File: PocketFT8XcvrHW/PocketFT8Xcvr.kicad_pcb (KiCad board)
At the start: 4 copper layers, 101.6 x 69.9 mm, 58 parts, among them IC1 SI5351C-B-GM1, J1 HX8357D SPI, J2 22-23-2021, J3 GPS, J5 HX8357D 8-BIT, Q1 2N3904, Q2 2N3906, Q3 2N7000, Q4 2N7000, U1 MCP3422A1T-E/SN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

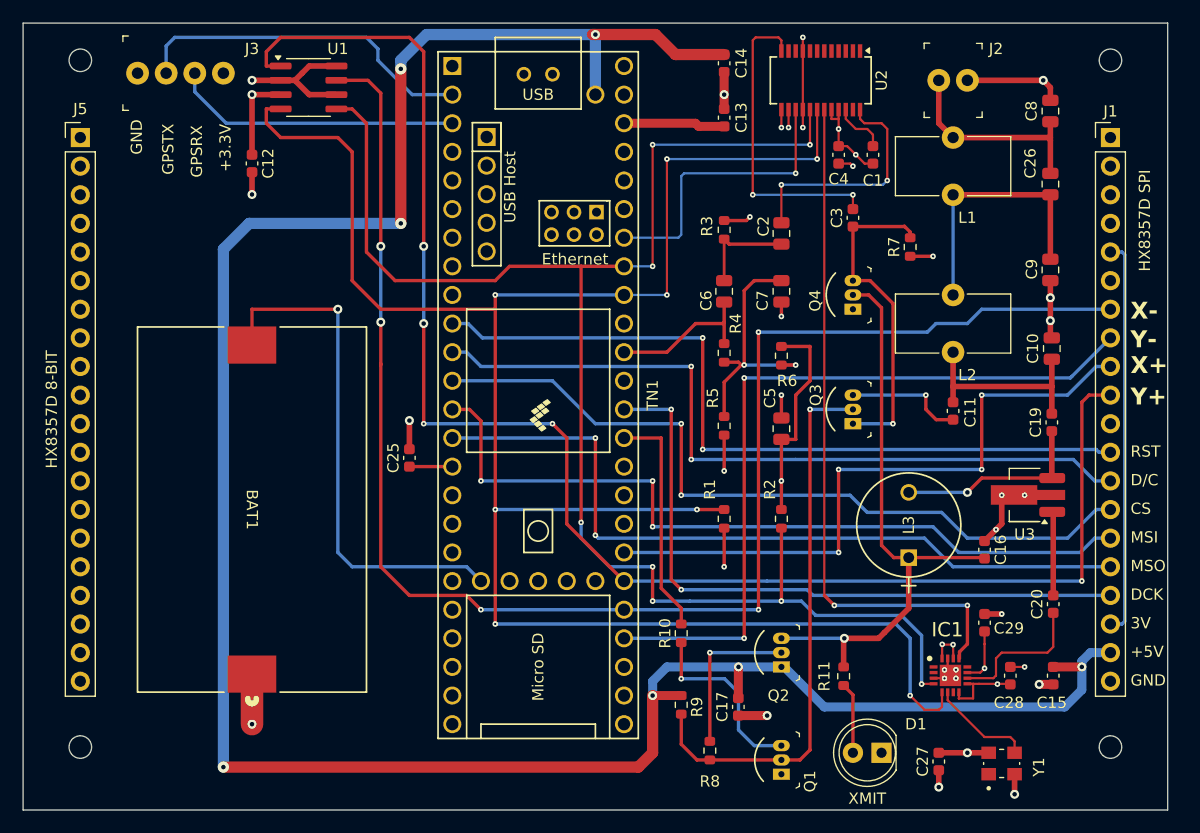
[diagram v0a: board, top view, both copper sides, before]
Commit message: Housecleaning after abandoning the QFN16 SI5351 package
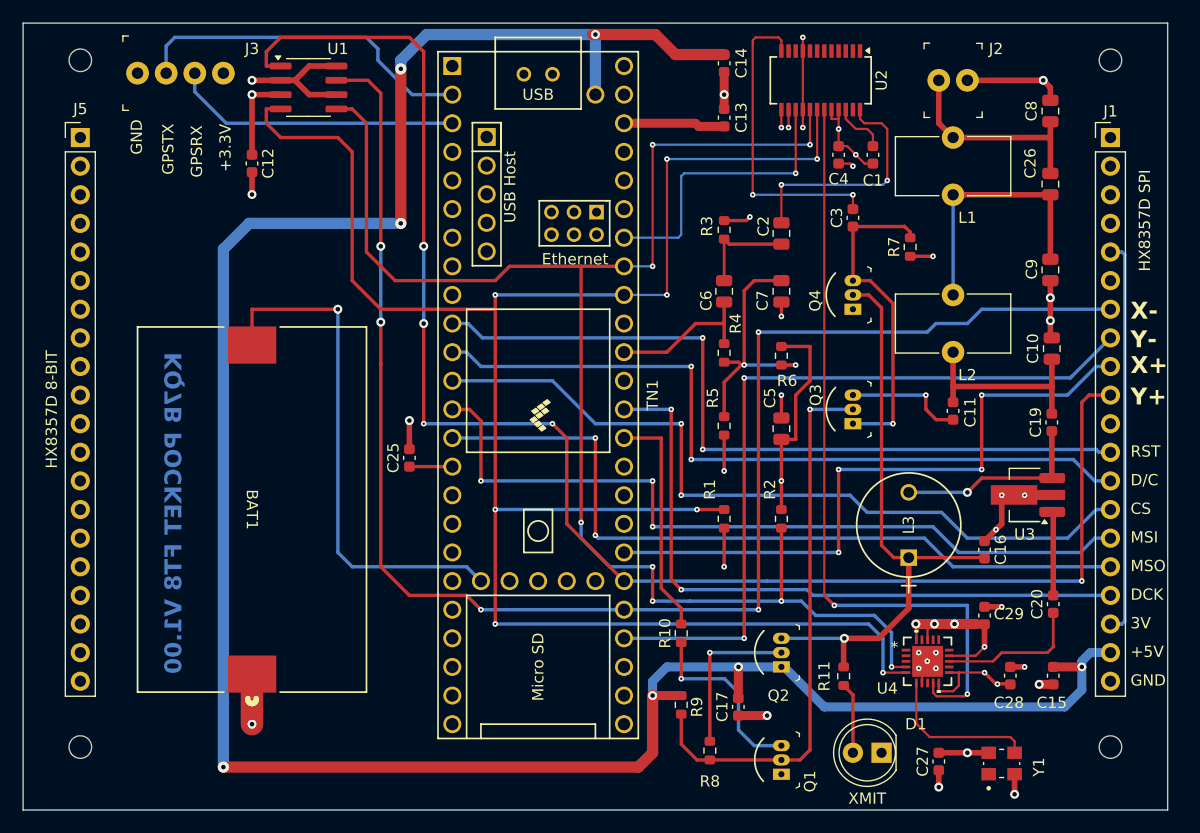
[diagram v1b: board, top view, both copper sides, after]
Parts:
- removed IC1: SI5351C-B-GM1, SI5351C-B-GM1:QFN50P300X300X90-17N-D
- added U4: SI5351C-B-GM, SI5351C-B-GM:QFN20_4X4_SKY, F.Cu at (181.9, 107.5)
- moved C29 0.63 mm to (186.9, 103.4)
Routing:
- net +3.3V: track 71.3 -> 79.9 mm, vias 10 -> 12
- net /SDA: track 178.1 -> 171.0 mm
- net /RCLK: track 61.2 -> 68.2 mm
- net Net-(U4-CLKIN): track 9.17 -> 14.0 mm
- net /SCL: track 141.1 -> 137.2 mm
- net GND: track 80.7 -> 80.0 mm, vias 31 -> 32
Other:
- board text added: "KQ7B POCKET FT8 V1.00"

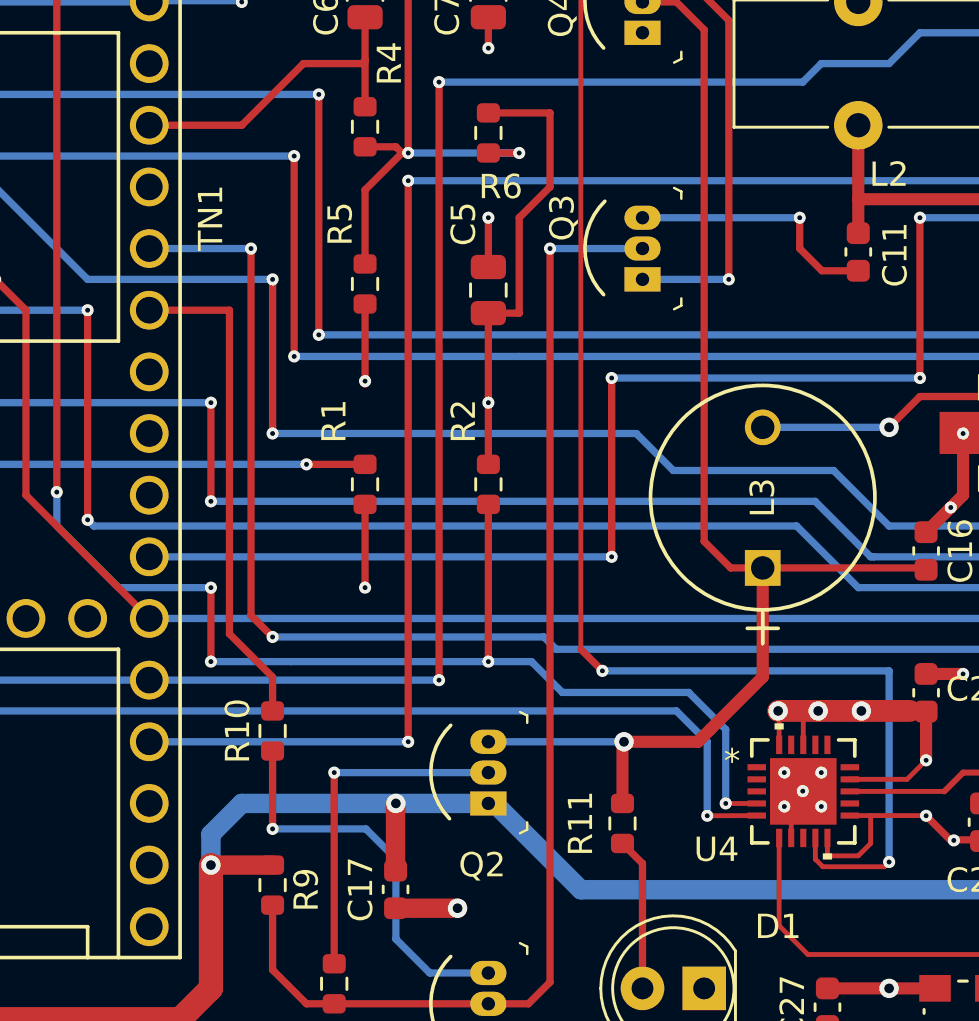
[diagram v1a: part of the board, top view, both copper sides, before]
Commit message: PCB Patch, test and FW changes to repair 1-v101-sck-and-ptt-reversed
SCK signal moved from digital pin 14 in Teensy 3.6 to pin 13 in Teensy 4.1.  Workaround PCB patch swaps pins 13 and 14.  Schematic, board layout, tests and FW updated for revised pin assignments.  Test03-Display now passes.
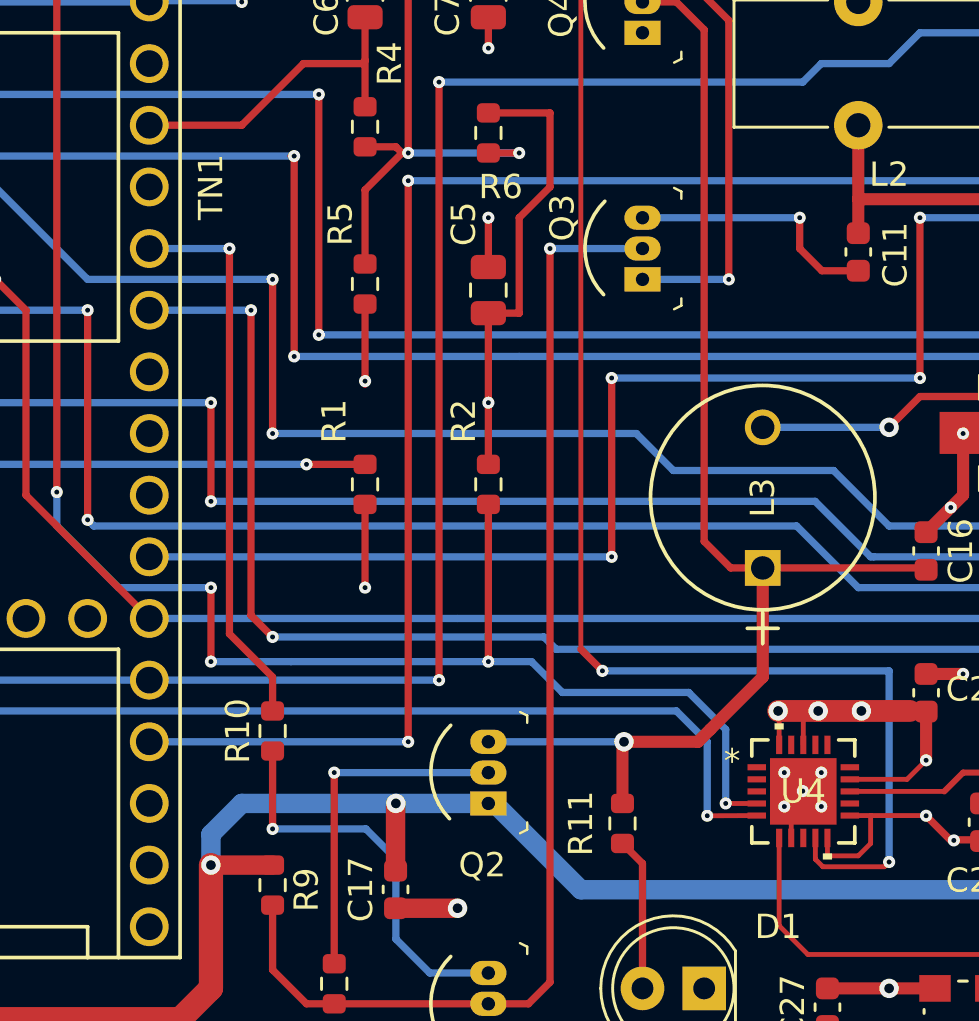
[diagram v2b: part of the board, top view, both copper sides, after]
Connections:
- TN1 pad 35: /PTT -> /DCLK
- TN1 pad 36: /DCLK -> /PTT
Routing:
- net /PTT: track 20.5 -> 23.1 mm, vias 0 -> 1
- net /DCLK: track 58.9 -> 56.3 mm

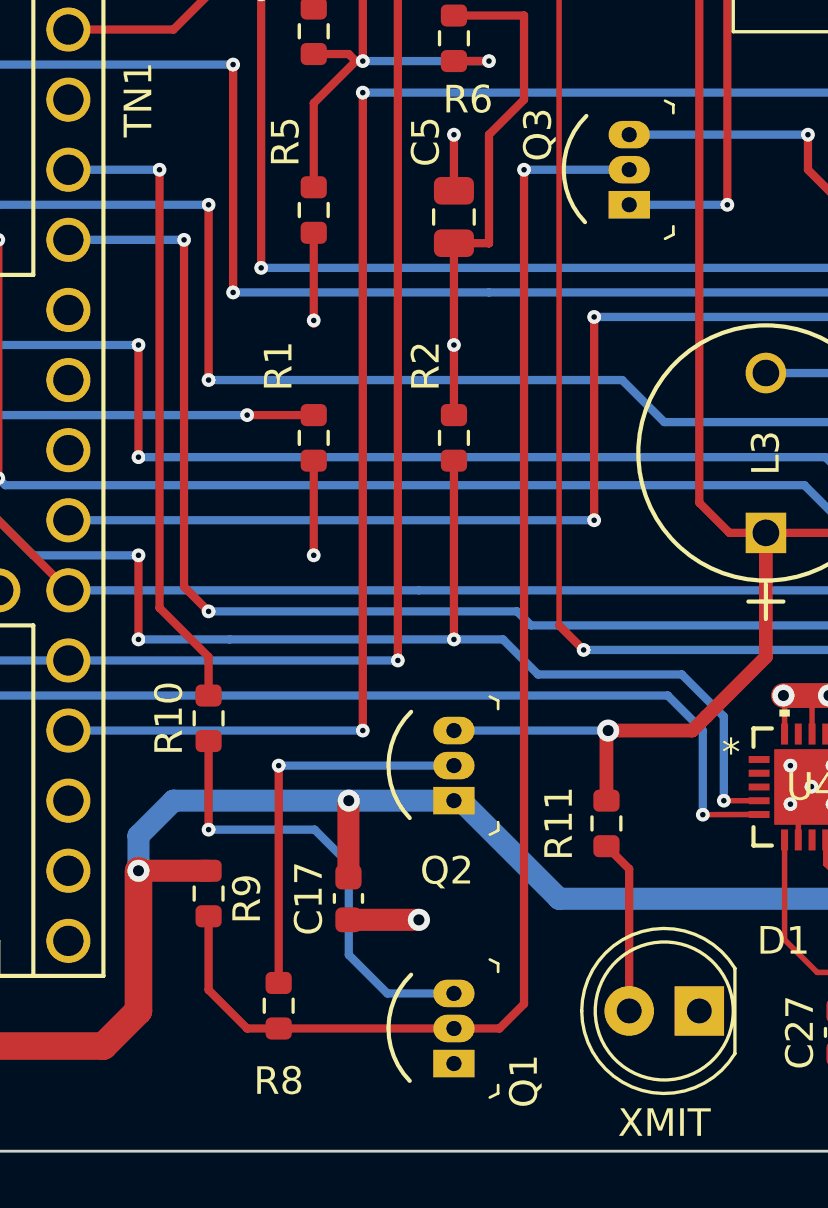
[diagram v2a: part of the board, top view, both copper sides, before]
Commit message: Fixed XMIT LED is always "on" and cannot be turned-off
The digikey 2N3904 symbol reversed the pin numbers for B and C.  This commit includes the schematic with the corrected symbol.
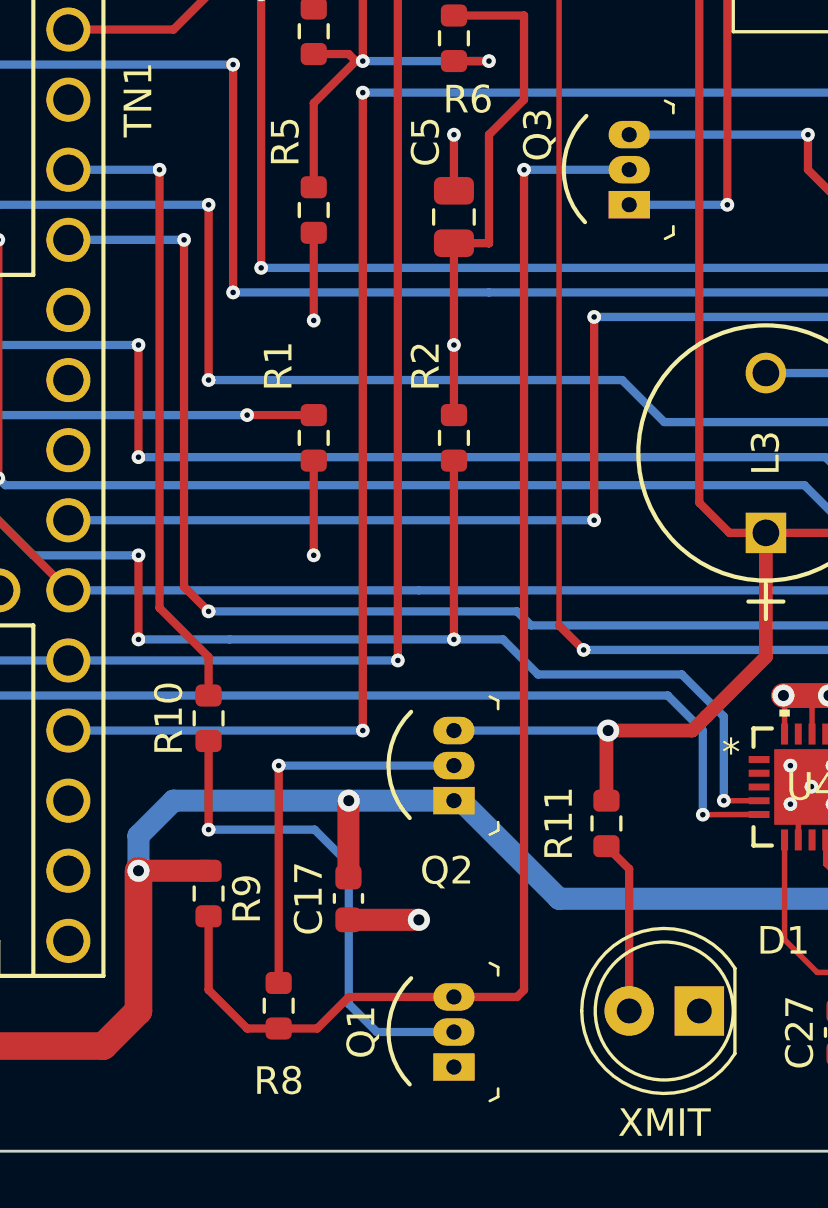
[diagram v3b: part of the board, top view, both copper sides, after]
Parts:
- moved Q1 0.13 mm to (168.9, 117.6)
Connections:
- Q1 pad 2: /RECV -> Net-(Q1-B)
- Q1 pad 3: Net-(Q1-B) -> /RECV
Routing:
- net Net-(Q1-B): track 16.5 -> 18.1 mm

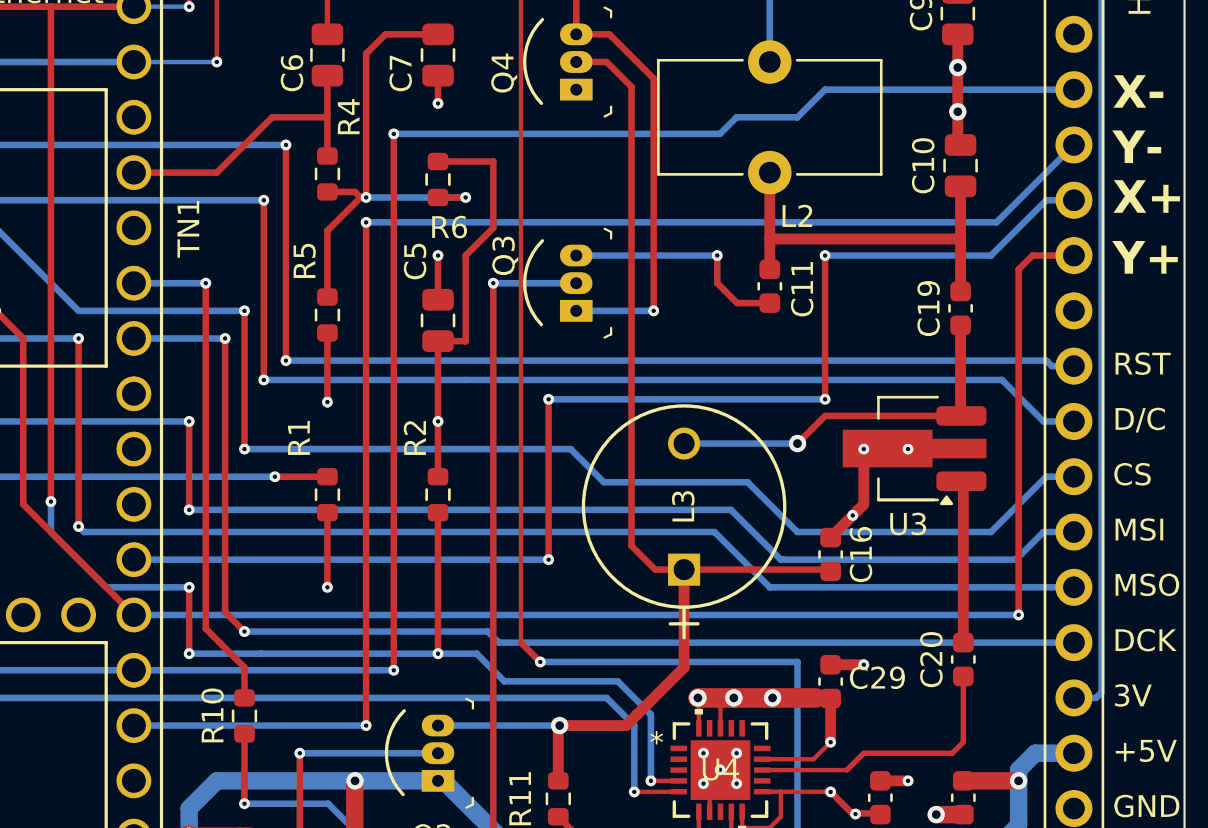
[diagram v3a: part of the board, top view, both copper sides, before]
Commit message: Resolved:  Touchpad needs coordination over full screen #8
Added R12 and R13 to lower the driven voltage to the touchpad so that it lies below the MCP3422's 2.048 Volt reference.
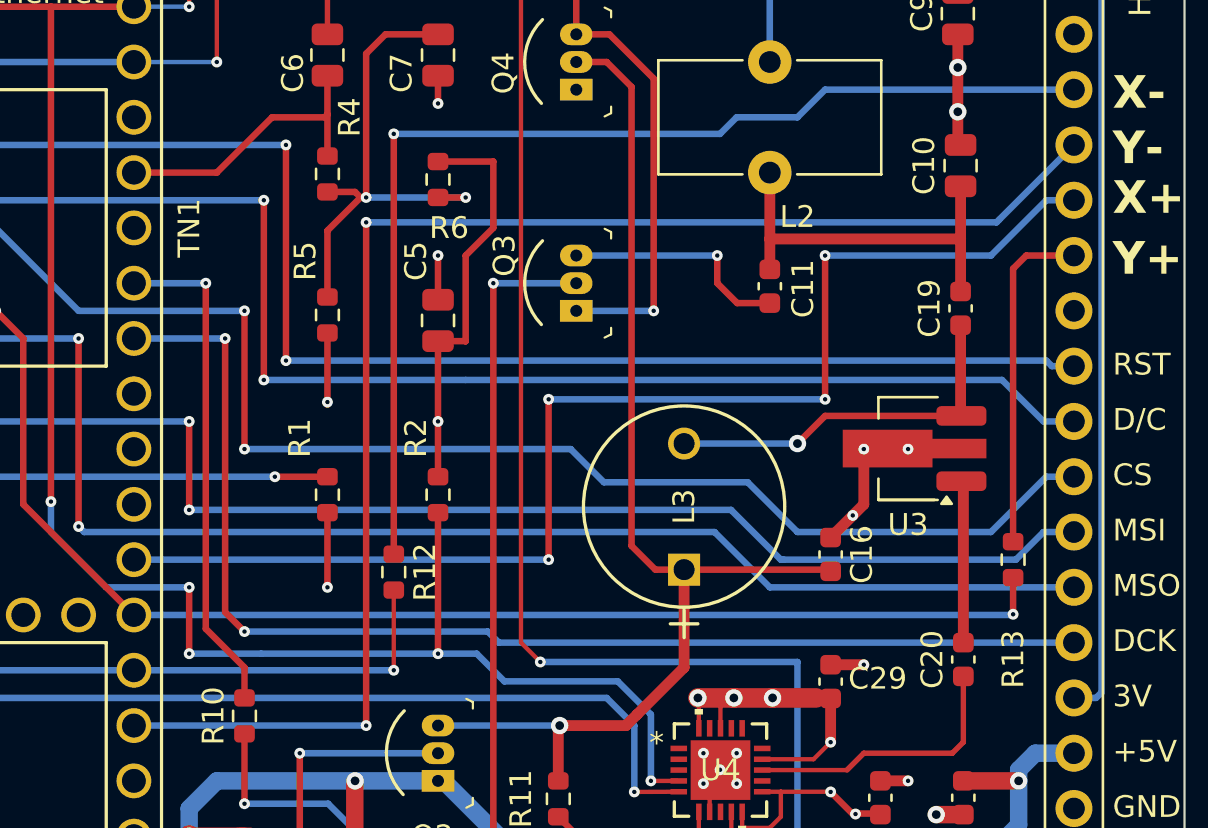
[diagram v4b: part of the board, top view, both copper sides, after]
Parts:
- added R12: 510, Resistor_SMD:R_0603_1608Metric, F.Cu at (166.9, 98.4)
- added R13: 510, Resistor_SMD:R_0603_1608Metric, F.Cu at (195.3, 97.8)
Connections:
- J1 pad 10: /Y+ -> Net-(J1-Y+)
- J1 pad 7: /X- -> Net-(J1-X-)
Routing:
- net /X-: track 138.4 -> 85.4 mm, vias 5 -> 4
- net Net-(J1-X-): track 0.00 -> 51.4 mm, vias 0 -> 1
- net /Y+: track 138.0 -> 120.8 mm
- net Net-(J1-Y+): track 0.00 -> 15.6 mm

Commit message: Resolve V1.01 PCB is using the Teensy 3.X rather than 4.X audio input network on pin A2 #15
Resolution modifies V1.01 schematic to replace 10K R6 with 2.2K Ohms per Teensy Audio System Design Tool documentation for ADC input on Teensy 4.1.
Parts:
- R6: value 10K -> 2.2K
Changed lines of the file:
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@@
 		(fp_text user "*"
 			(at -1.5367 -1.243965 0)
+			(unlocked yes)
 			(layer "F.Fab")
 			(effects
@@
 		(fp_text user "*"
 			(at -1.5367 -1.243965 0)
-			(unlocked yes)
 			(layer "F.Fab")
 			(effects
@@
 			)
 		)
-		(property "Value" "10K"
+		(property "Value" "2.2K"
 			(at 0 1.43 90)
 			(layer "F.Fab")
@@
 			)
 		)
-		(property "Datasheet" "https://www.vishay.com/docs/20035/dcrcwe3.pdf"
+		(property "Datasheet" ""
 			(at 0 0 90)
 			(unlocked yes)
@@
 			)
 		)
-		(property "Description" "RES 47.0K OHM 1/8W 0805 SMD"
+		(property "Description" ""
 			(at 0 0 90)
 			(unlocked yes)
@@
 			)
 		)
-		(property "PROD_ID" "RES-00824"
+		(property "PROD_ID" ""
 			(at 0 0 90)
 			(unlocked yes)
@@
 			)
 		)
-		(property "Mfg Part #" "RC0603JR-0710KL"
+		(property "Mfg Part #" ""
 			(at 0 0 90)
 			(unlocked yes)
